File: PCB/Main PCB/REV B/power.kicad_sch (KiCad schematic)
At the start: 14 parts, among them U5 AMS1117-3.3, U6 TPS2115APWR

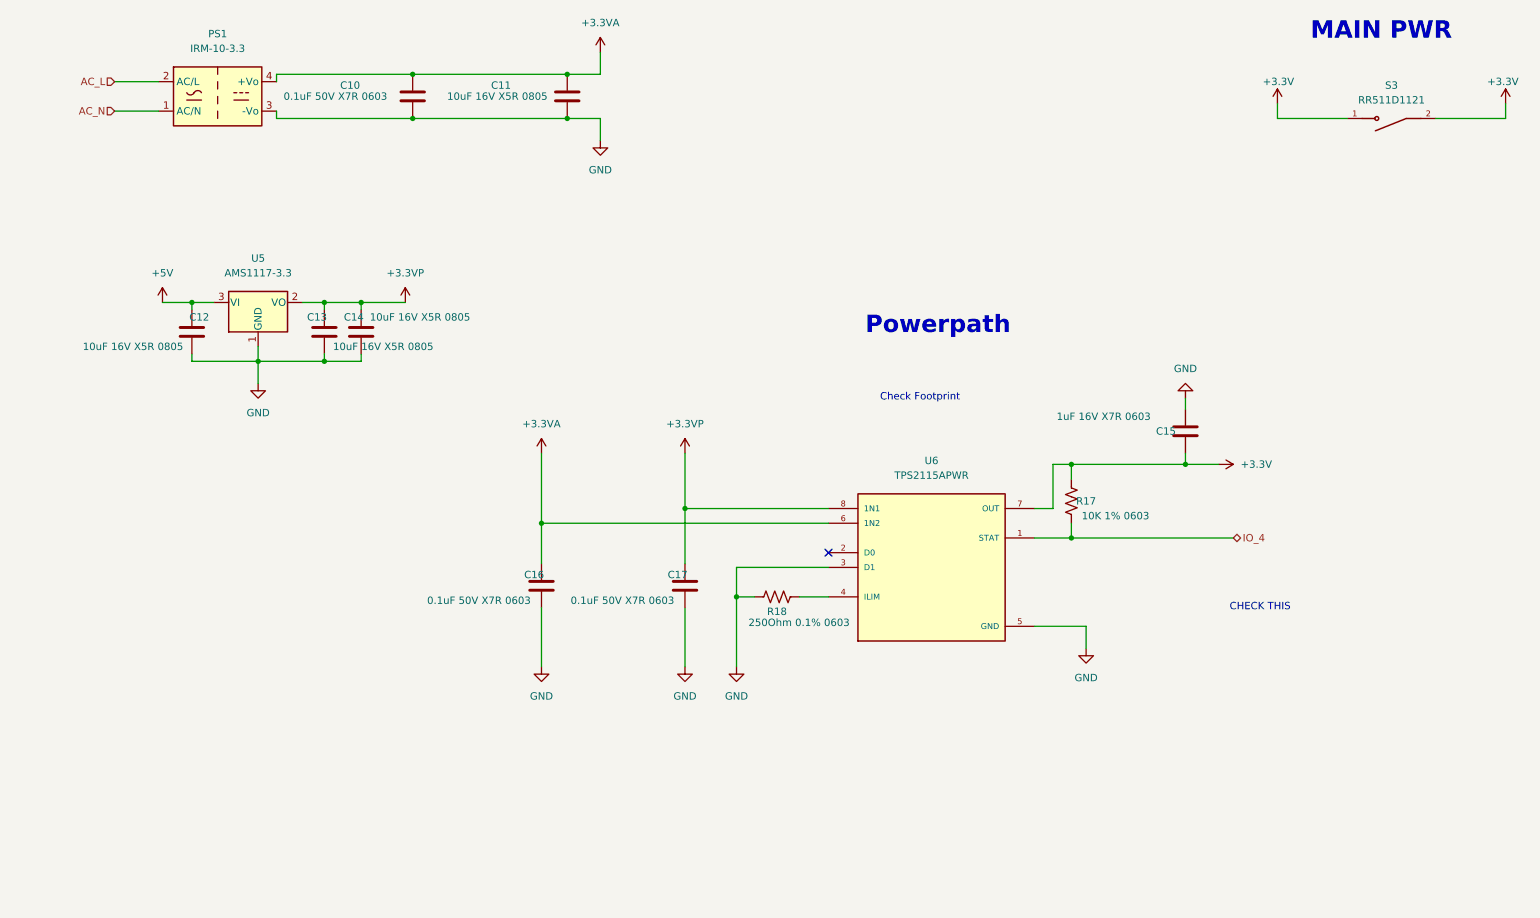
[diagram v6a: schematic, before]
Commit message: SD card complete. All gpio full
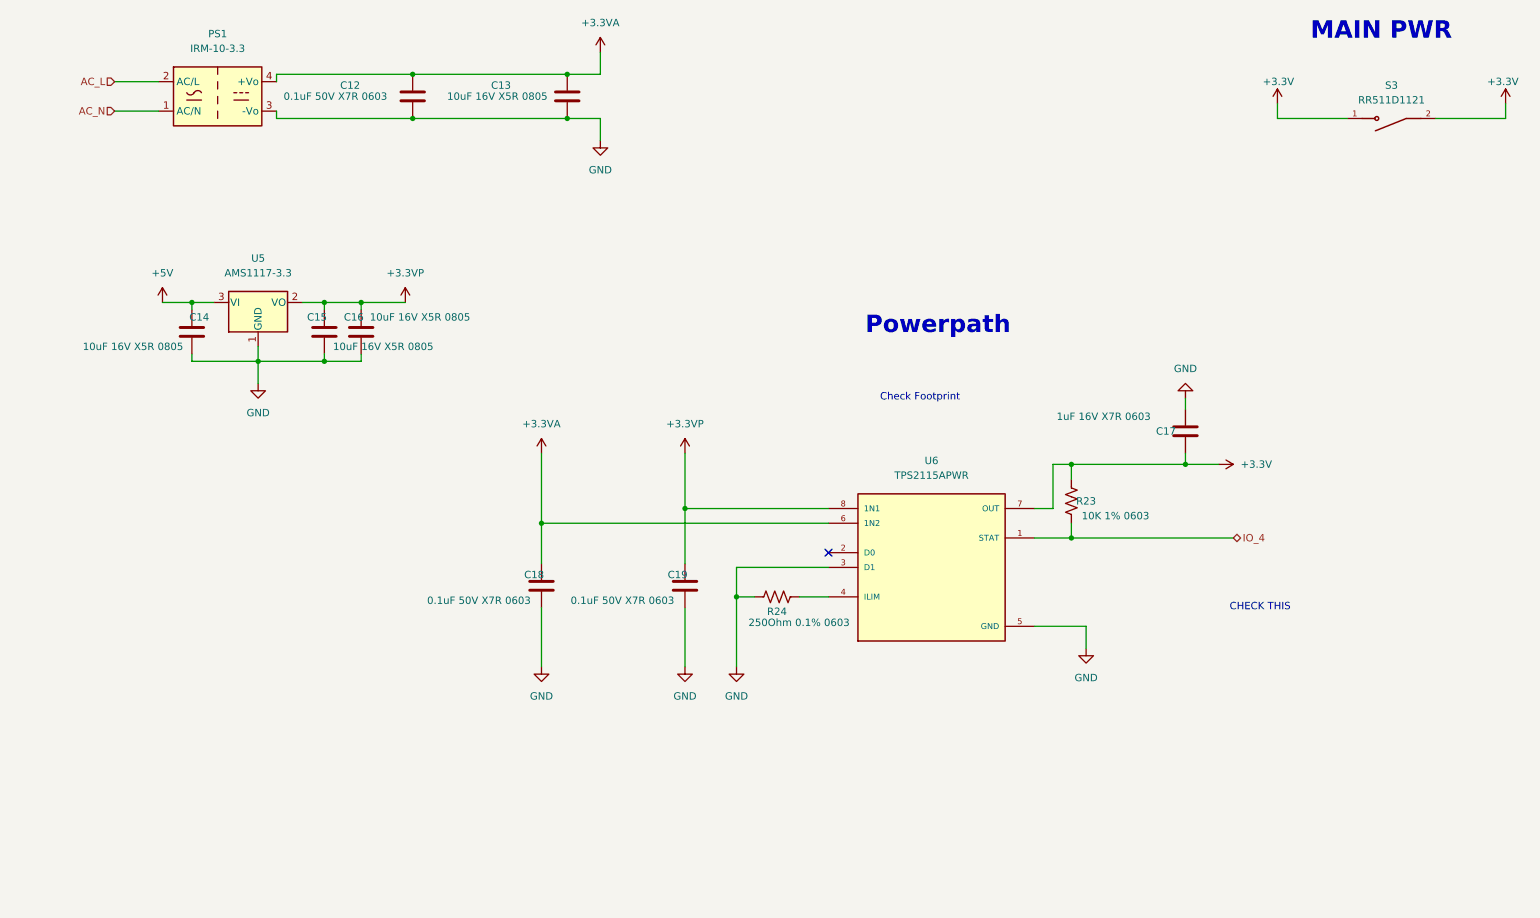
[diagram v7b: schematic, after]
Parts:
- renumbered C10 to C12, C11 to C13, C12 to C14, C13 to C15, C14 to C16, C15 to C17, C16 to C18, C17 to C19, R17 to R23, R18 to R24
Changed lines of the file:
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@@
   (symbol (lib_id "power:+3.3VP") (at 130.175 104.775 0) (unit 1)
     (in_bom yes) (on_board yes) (fields_autoplaced)
-    (property "Reference" "#PWR056" (id 0) (at 133.985 106.045 0)
+    (property "Reference" "#PWR065" (id 0) (at 133.985 106.045 0)
       (effects (font (size 1.27 1.27)) hide)
     )
@@
   (symbol (lib_id "power:GND") (at 56.515 92.71 0) (unit 1)
     (in_bom yes) (on_board yes)
-    (property "Reference" "#PWR053" (id 0) (at 56.515 99.06 0)
+    (property "Reference" "#PWR062" (id 0) (at 56.515 99.06 0)
       (effects (font (size 1.27 1.27)) hide)
     )
@@
   (symbol (lib_id "power:GND") (at 105.41 141.605 0) (unit 1)
     (in_bom yes) (on_board yes) (fields_autoplaced)
-    (property "Reference" "#PWR059" (id 0) (at 105.41 147.955 0)
+    (property "Reference" "#PWR068" (id 0) (at 105.41 147.955 0)
       (effects (font (size 1.27 1.27)) hide)
     )
@@
   (symbol (lib_id "power:GND") (at 139.065 141.605 0) (unit 1)
     (in_bom yes) (on_board yes) (fields_autoplaced)
-    (property "Reference" "#PWR061" (id 0) (at 139.065 147.955 0)
+    (property "Reference" "#PWR070" (id 0) (at 139.065 147.955 0)
       (effects (font (size 1.27 1.27)) hide)
     )
@@
   (symbol (lib_id "Device:C") (at 109.855 43.18 0) (mirror y) (unit 1)
     (in_bom yes) (on_board yes)
-    (property "Reference" "C11" (id 0) (at 98.425 41.275 0))
+    (property "Reference" "C13" (id 0) (at 98.425 41.275 0))
     (property "Value" "10uF 16V X5R 0805" (id 1) (at 97.79 43.18 0))
     (property "Footprint" "Capacitor_SMD:C_0805_2012Metric" (id 2) (at 108.8898 46.99 0)
@@
   (symbol (lib_id "Device:R_US") (at 146.05 129.54 270) (unit 1)
     (in_bom yes) (on_board yes)
-    (property "Reference" "R18" (id 0) (at 146.05 132.08 90))
+    (property "Reference" "R24" (id 0) (at 146.05 132.08 90))
     (property "Value" "250Ohm 0.1% 0603" (id 1) (at 149.86 133.985 90))
     (property "Footprint" "Resistor_SMD:R_0603_1608Metric" (id 2) (at 145.796 130.556 90)
@@
   (symbol (lib_id "Device:R_US") (at 196.85 113.03 0) (unit 1)
     (in_bom yes) (on_board yes)
-    (property "Reference" "R17" (id 0) (at 199.39 113.03 0))
+    (property "Reference" "R23" (id 0) (at 199.39 113.03 0))
     (property "Value" "10K 1% 0603" (id 1) (at 204.47 115.57 0))
     (property "Footprint" "Resistor_SMD:R_0603_1608Metric" (id 2) (at 197.866 113.284 90)
@@
   (symbol (lib_id "Device:C") (at 130.175 127.635 0) (mirror x) (unit 1)
     (in_bom yes) (on_board yes)
-    (property "Reference" "C17" (id 0) (at 128.905 125.73 0))
+    (property "Reference" "C19" (id 0) (at 128.905 125.73 0))
     (property "Value" "0.1uF 50V X7R 0603" (id 1) (at 119.38 130.175 0))
     (property "Footprint" "Capacitor_SMD:C_0603_1608Metric" (id 2) (at 131.1402 123.825 0)
@@
   (symbol (lib_id "Device:C") (at 67.945 83.82 0) (mirror y) (unit 1)
     (in_bom yes) (on_board yes)
-    (property "Reference" "C13" (id 0) (at 66.675 81.28 0))
+    (property "Reference" "C15" (id 0) (at 66.675 81.28 0))
     (property "Value" "10uF 16V X5R 0805" (id 1) (at 78.105 86.36 0))
     (property "Footprint" "Capacitor_SMD:C_0805_2012Metric" (id 2) (at 66.9798 87.63 0)
@@
   (symbol (lib_id "power:+5V") (at 40.005 78.74 0) (unit 1)
     (in_bom yes) (on_board yes) (fields_autoplaced)
-    (property "Reference" "#PWR051" (id 0) (at 40.005 82.55 0)
+    (property "Reference" "#PWR060" (id 0) (at 40.005 82.55 0)
       (effects (font (size 1.27 1.27)) hide)
     )
@@
   (symbol (lib_id "power:+3.3V") (at 222.25 106.68 270) (unit 1)
     (in_bom yes) (on_board yes) (fields_autoplaced)
-    (property "Reference" "#PWR057" (id 0) (at 218.44 106.68 0)
+    (property "Reference" "#PWR066" (id 0) (at 218.44 106.68 0)
       (effects (font (size 1.27 1.27)) hide)
     )
@@
   (symbol (lib_id "power:+3.3V") (at 232.41 44.45 0) (mirror y) (unit 1)
     (in_bom yes) (on_board yes)
-    (property "Reference" "#PWR048" (id 0) (at 232.41 48.26 0)
+    (property "Reference" "#PWR057" (id 0) (at 232.41 48.26 0)
       (effects (font (size 1.27 1.27)) hide)
     )
@@
   (symbol (lib_id "Device:C") (at 45.085 83.82 0) (unit 1)
     (in_bom yes) (on_board yes)
-    (property "Reference" "C12" (id 0) (at 46.355 81.28 0))
+    (property "Reference" "C14" (id 0) (at 46.355 81.28 0))
     (property "Value" "10uF 16V X5R 0805" (id 1) (at 34.925 86.36 0))
     (property "Footprint" "Capacitor_SMD:C_0805_2012Metric" (id 2) (at 46.0502 87.63 0)
@@
   (symbol (lib_id "Device:C") (at 74.295 83.82 0) (mirror y) (unit 1)
     (in_bom yes) (on_board yes)
-    (property "Reference" "C14" (id 0) (at 73.025 81.28 0))
+    (property "Reference" "C16" (id 0) (at 73.025 81.28 0))
     (property "Value" "10uF 16V X5R 0805" (id 1) (at 84.455 81.28 0))
     (property "Footprint" "Capacitor_SMD:C_0805_2012Metric" (id 2) (at 73.3298 87.63 0)
@@
   (symbol (lib_id "power:+3.3VA") (at 105.41 104.775 0) (unit 1)
     (in_bom yes) (on_board yes) (fields_autoplaced)
-    (property "Reference" "#PWR055" (id 0) (at 105.41 108.585 0)
+    (property "Reference" "#PWR064" (id 0) (at 105.41 108.585 0)
       (effects (font (size 1.27 1.27)) hide)
     )
@@
   (symbol (lib_id "power:GND") (at 115.57 50.8 0) (unit 1)
     (in_bom yes) (on_board yes)
-    (property "Reference" "#PWR050" (id 0) (at 115.57 57.15 0)
+    (property "Reference" "#PWR059" (id 0) (at 115.57 57.15 0)
       (effects (font (size 1.27 1.27)) hide)
     )
@@
   (symbol (lib_id "Device:C") (at 105.41 127.635 0) (mirror x) (unit 1)
     (in_bom yes) (on_board yes)
-    (property "Reference" "C16" (id 0) (at 104.14 125.73 0))
+    (property "Reference" "C18" (id 0) (at 104.14 125.73 0))
     (property "Value" "0.1uF 50V X7R 0603" (id 1) (at 94.615 130.175 0))
     (property "Footprint" "Capacitor_SMD:C_0603_1608Metric" (id 2) (at 106.3752 123.825 0)
@@
   (symbol (lib_id "power:+3.3VP") (at 81.915 78.74 0) (unit 1)
     (in_bom yes) (on_board yes) (fields_autoplaced)
-    (property "Reference" "#PWR052" (id 0) (at 85.725 80.01 0)
+    (property "Reference" "#PWR061" (id 0) (at 85.725 80.01 0)
       (effects (font (size 1.27 1.27)) hide)
     )
@@
   (symbol (lib_id "power:GND") (at 216.535 95.25 180) (unit 1)
     (in_bom yes) (on_board yes) (fields_autoplaced)
-    (property "Reference" "#PWR054" (id 0) (at 216.535 88.9 0)
+    (property "Reference" "#PWR063" (id 0) (at 216.535 88.9 0)
       (effects (font (size 1.27 1.27)) hide)
     )
@@
   (symbol (lib_id "power:GND") (at 199.39 138.43 0) (unit 1)
     (in_bom yes) (on_board yes) (fields_autoplaced)
-    (property "Reference" "#PWR058" (id 0) (at 199.39 144.78 0)
+    (property "Reference" "#PWR067" (id 0) (at 199.39 144.78 0)
       (effects (font (size 1.27 1.27)) hide)
     )
@@
   (symbol (lib_id "power:GND") (at 130.175 141.605 0) (unit 1)
     (in_bom yes) (on_board yes) (fields_autoplaced)
-    (property "Reference" "#PWR060" (id 0) (at 130.175 147.955 0)
+    (property "Reference" "#PWR069" (id 0) (at 130.175 147.955 0)
       (effects (font (size 1.27 1.27)) hide)
     )
@@
   (symbol (lib_id "Device:C") (at 216.535 100.965 0) (unit 1)
     (in_bom yes) (on_board yes)
-    (property "Reference" "C15" (id 0) (at 211.455 100.965 0)
+    (property "Reference" "C17" (id 0) (at 211.455 100.965 0)
       (effects (font (size 1.27 1.27)) (justify left))
     )
@@
   (symbol (lib_id "Device:C") (at 83.185 43.18 0) (mirror x) (unit 1)
     (in_bom yes) (on_board yes)
-    (property "Reference" "C10" (id 0) (at 72.39 41.275 0))
+    (property "Reference" "C12" (id 0) (at 72.39 41.275 0))
     (property "Value" "0.1uF 50V X7R 0603" (id 1) (at 69.85 43.18 0))
     (property "Footprint" "Capacitor_SMD:C_0603_1608Metric" (id 2) (at 84.1502 39.37 0)
@@
   (symbol (lib_id "power:+3.3V") (at 271.78 44.45 0) (mirror y) (unit 1)
     (in_bom yes) (on_board yes)
-    (property "Reference" "#PWR049" (id 0) (at 271.78 48.26 0)
+    (property "Reference" "#PWR058" (id 0) (at 271.78 48.26 0)
       (effects (font (size 1.27 1.27)) hide)
     )
@@
   (symbol (lib_id "power:+3.3VA") (at 115.57 35.56 0) (unit 1)
     (in_bom yes) (on_board yes) (fields_autoplaced)
-    (property "Reference" "#PWR047" (id 0) (at 115.57 39.37 0)
-      (effects (font (size 1.27 1.27)) hide)
-    )
+    (property "Reference" "#PWR056" (id 0) (at 115.57 39.37 0)
+      (effects (font (size 1.27 1.27)) hide)
+    )

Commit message: Begin layout Rev B PCB
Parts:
- renumbered C12 to C13, C13 to C14, C14 to C15, C15 to C16, C16 to C17, C17 to C18, C18 to C19, C19 to C20
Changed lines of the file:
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@@
   (symbol (lib_id "Device:C") (at 109.855 43.18 0) (mirror y) (unit 1)
     (in_bom yes) (on_board yes)
-    (property "Reference" "C13" (id 0) (at 98.425 41.275 0))
+    (property "Reference" "C14" (id 0) (at 98.425 41.275 0))
     (property "Value" "10uF 16V X5R 0805" (id 1) (at 97.79 43.18 0))
     (property "Footprint" "Capacitor_SMD:C_0805_2012Metric" (id 2) (at 108.8898 46.99 0)
@@
   (symbol (lib_id "Device:C") (at 130.175 127.635 0) (mirror x) (unit 1)
     (in_bom yes) (on_board yes)
-    (property "Reference" "C19" (id 0) (at 128.905 125.73 0))
+    (property "Reference" "C20" (id 0) (at 128.905 125.73 0))
     (property "Value" "0.1uF 50V X7R 0603" (id 1) (at 119.38 130.175 0))
     (property "Footprint" "Capacitor_SMD:C_0603_1608Metric" (id 2) (at 131.1402 123.825 0)
@@
   (symbol (lib_id "Device:C") (at 67.945 83.82 0) (mirror y) (unit 1)
     (in_bom yes) (on_board yes)
-    (property "Reference" "C15" (id 0) (at 66.675 81.28 0))
+    (property "Reference" "C16" (id 0) (at 66.675 81.28 0))
     (property "Value" "10uF 16V X5R 0805" (id 1) (at 78.105 86.36 0))
     (property "Footprint" "Capacitor_SMD:C_0805_2012Metric" (id 2) (at 66.9798 87.63 0)
@@
   (symbol (lib_id "Device:C") (at 45.085 83.82 0) (unit 1)
     (in_bom yes) (on_board yes)
-    (property "Reference" "C14" (id 0) (at 46.355 81.28 0))
+    (property "Reference" "C15" (id 0) (at 46.355 81.28 0))
     (property "Value" "10uF 16V X5R 0805" (id 1) (at 34.925 86.36 0))
     (property "Footprint" "Capacitor_SMD:C_0805_2012Metric" (id 2) (at 46.0502 87.63 0)
@@
   (symbol (lib_id "Device:C") (at 74.295 83.82 0) (mirror y) (unit 1)
     (in_bom yes) (on_board yes)
-    (property "Reference" "C16" (id 0) (at 73.025 81.28 0))
+    (property "Reference" "C17" (id 0) (at 73.025 81.28 0))
     (property "Value" "10uF 16V X5R 0805" (id 1) (at 84.455 81.28 0))
     (property "Footprint" "Capacitor_SMD:C_0805_2012Metric" (id 2) (at 73.3298 87.63 0)
@@
   (symbol (lib_id "Device:C") (at 105.41 127.635 0) (mirror x) (unit 1)
     (in_bom yes) (on_board yes)
-    (property "Reference" "C18" (id 0) (at 104.14 125.73 0))
+    (property "Reference" "C19" (id 0) (at 104.14 125.73 0))
     (property "Value" "0.1uF 50V X7R 0603" (id 1) (at 94.615 130.175 0))
     (property "Footprint" "Capacitor_SMD:C_0603_1608Metric" (id 2) (at 106.3752 123.825 0)
@@
   (symbol (lib_id "Device:C") (at 216.535 100.965 0) (unit 1)
     (in_bom yes) (on_board yes)
-    (property "Reference" "C17" (id 0) (at 211.455 100.965 0)
+    (property "Reference" "C18" (id 0) (at 211.455 100.965 0)
       (effects (font (size 1.27 1.27)) (justify left))
     )
@@
   (symbol (lib_id "Device:C") (at 83.185 43.18 0) (mirror x) (unit 1)
     (in_bom yes) (on_board yes)
-    (property "Reference" "C12" (id 0) (at 72.39 41.275 0))
+    (property "Reference" "C13" (id 0) (at 72.39 41.275 0))
     (property "Value" "0.1uF 50V X7R 0603" (id 1) (at 69.85 43.18 0))
     (property "Footprint" "Capacitor_SMD:C_0603_1608Metric" (id 2) (at 84.1502 39.37 0)
